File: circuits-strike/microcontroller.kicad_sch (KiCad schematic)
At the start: 10 parts, among them U1 ESP32-WROOM-32

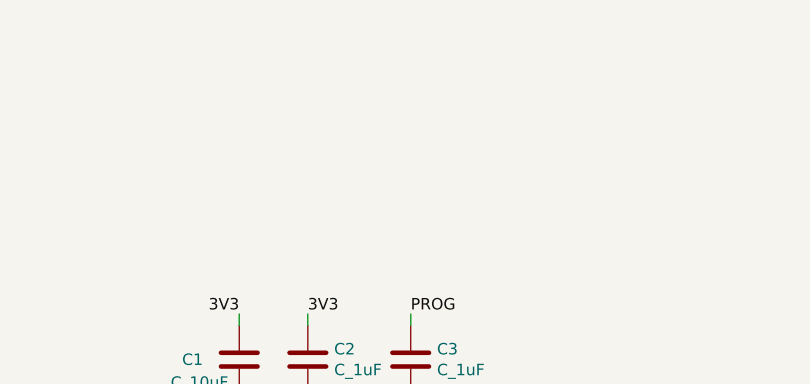
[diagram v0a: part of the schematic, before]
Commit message: Finished schematic for shrinking PCB for residential systems
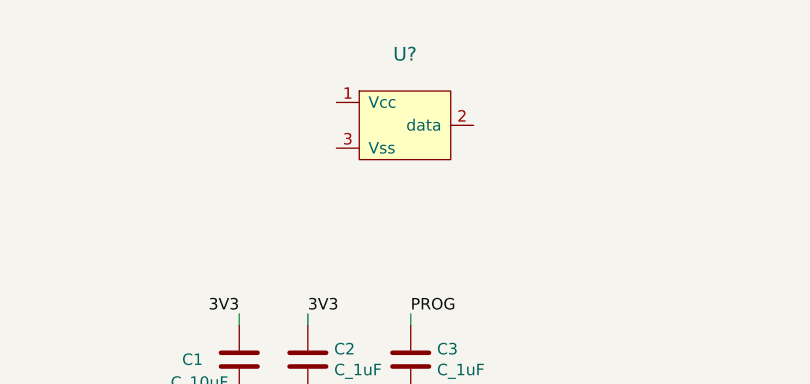
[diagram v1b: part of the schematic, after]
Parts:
- added U?: (no value), symbol Open Automation:PIR-DIGITAL
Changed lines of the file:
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@@
     (pin "2")
   )
+  (symbol (lib_id "Open Automation:PIR-DIGITAL") (at 121.285 32.385 0) (unit 1)
+    (in_bom yes) (on_board yes) (fields_autoplaced)
+    (property "Reference" "U?" (id 0) (at 122.555 25.7609 0)
+      (effects (font (size 1.524 1.524)))
+    )
+    (property "Value" "" (id 1) (at 122.555 28.7543 0)
+      (effects (font (size 1.524 1.524)))
+    )
+    (property "Footprint" "" (id 2) (at 122.555 43.815 0)
+      (effects (font (size 1.524 1.524)) hide)
+    )
+    (property "Datasheet" "http://unusualelectronics.co.uk/wordpress/wp-content/uploads/Pir-AS312.pdf" (id 3) (at 123.825 41.275 0)
+      (effects (font (size 1.524 1.524)) hide)
+    )
+    (property "Part Number" "PYQ2898" (id 4) (at 121.285 46.355 0)
+      (effects (font (size 1.524 1.524)) hide)
+    )
+    (pin "1")
+    (pin "2")
+    (pin "3")
+  )
 )
